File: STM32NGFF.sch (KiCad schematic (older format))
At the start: 30 parts, among them J1 USB_C_Receptacle_USB2.0, J2 2199119-4, U1 MIC5205-3.3YM5, U2 STM32F303CCTx, U3 USBLC6-2SC6, Y1 16MHz

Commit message: Add Correct M.2 Connector, and switch MCU to STM32F303RBTx
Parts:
- removed U2: STM32F303CCTx, Package_QFP:LQFP-48_7x7mm_P0.5mm, symbol MCU_ST_STM32F3:STM32F303CCTx
- added C11: 100n, Capacitor_SMD:C_0603_1608Metric, symbol Device:C_Small
- added U2: STM32F303RBTx, Package_QFP:LQFP-64_10x10mm_P0.5mm, symbol MCU_ST_STM32F3:STM32F303RBTx
- J2: symbol TE_2199119-4:2199119-4 -> Argosy~Research:NASM0-S6701-TP40
- renumbered C3 to C10, C11 to C12, C12 to C13, C4 to C3, C6 to C4, C7 to C6, C8 to C7, C9 to C8, C10 to C9
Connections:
- net labels added: PC0, PC1, PC10, PC11, PC12, PC13, PC4, PC5, PC6, PC7, PC8, PC9, PD2, PF4
- net labels removed: NRST
- wire segments 163 -> 196
- no-connect marks 3 -> 4
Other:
- moved on the sheet: C1, C10, C12, C13, C2, C3, C4, C5, C6, C7, C8, C9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

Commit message: Routed and shaped PCB
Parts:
- removed C10: 10uf, Capacitor_SMD:C_0603_1608Metric, symbol Device:C_Small
- removed C4: 100nF, Capacitor_SMD:C_0603_1608Metric, symbol Device:C_Small
- removed J1: USB_C_Receptacle_USB2.0, Connector_USB:USB_C_Receptacle_HRO_TYPE-C-31-M-12, symbol Connector:USB_C_Receptacle_USB2.0
- added C12, C7: 100nF, Capacitor_SMD:C_0603_1608Metric, symbol Device:C_Small
- added C14: 10uf, Capacitor_SMD:C_0603_1608Metric, symbol Device:C_Small
- added J2, J4: S4B-PH-K-S(LF)(SN), JST:S4B-PH-K-S_LF_SN, symbol JST:S4B-PH-K-S(LF)(SN)
- added J3: HRO_TYPE-C-31-M-12, Type-C:HRO-TYPE-C-31-M-12-Assembly, symbol Type-C:HRO-TYPE-C-31-M-12
- added R7: 5.11k, Capacitor_SMD:C_0603_1608Metric, symbol Device:R_Small
- added R8: 1M, Capacitor_SMD:C_0603_1608Metric, symbol Device:R_Small
- added U1: 74LVC1G17, Package_TO_SOT_SMD:SOT-23-5, symbol 74xGxx:74LVC1G17
- J1: renamed from J2; value 2199119-4 -> NASMO-S6701-TP40; footprint TE:TE_2199119-4 -> Argosy Research:NASMO-S6701-TP40; symbol Argosy~Research:NASM0-S6701-TP40 -> Argosy_Research:NASM0-S6701-TP40; Comment 2199119-4 -> NASMO-S6701-TP40
- R4: value 1M -> 470
- R5: value 5.11k -> 1M
- renumbered C11 to C10, C12 to C11, C5 to C4, C6 to C5, C7 to C6, U1 to U2, U2 to U3, U3 to U4
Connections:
- net labels added: LED_3V3, LED_5V, LED_DATA, PC2, VBUS
- net labels removed: PB13
- wire segments 196 -> 283
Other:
- note added: "Addressable LED Support"
- note added: "SOM USB JST Connector"
- note added: "USB Daughterboard"
- note removed: "USB ESD Protection"
- note removed: "USB-C Connection"
- moved on the sheet: C10, C11, C13, C3, C4, C5, C6, C8, C9, L1, U2, U4

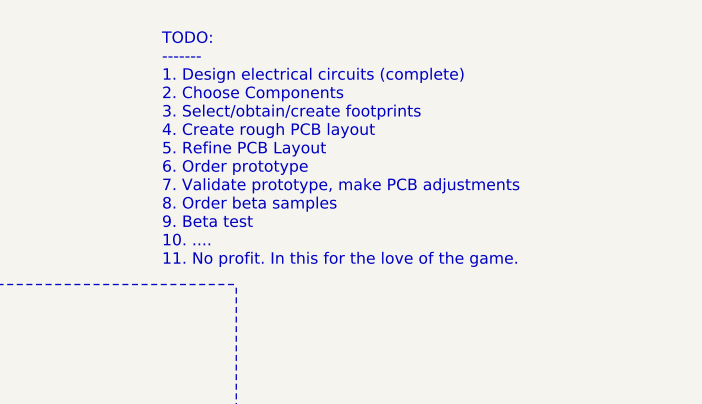
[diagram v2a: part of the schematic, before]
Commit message: Updated TODO list in schematic
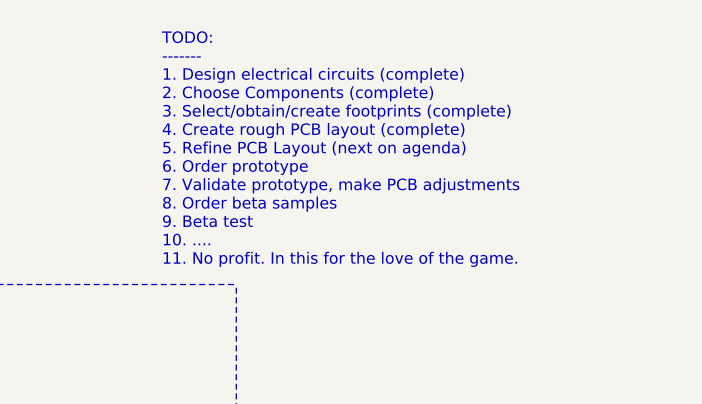
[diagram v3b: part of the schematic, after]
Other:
- note added: "TODO:\n-------\n1. Design electrical circuits (complete)\n2. Choose Components (complete)\n3. Select/obtain/create footprints (complete)\n4. Create rough PCB layout (complete)\n5. Refine PCB Layout (next on agenda)\n6. Order prototype\n7. Validate prototype, make PCB adjustments\n8. Order beta samples\n9. Beta test\n10. ....\n11. No profit. In this for the love of the game."
- note removed: "TODO:\n-------\n1. Design electrical circuits (complete)\n2. Choose Components\n3. Select/obtain/create footprints\n4. Create rough PCB layout\n5. Refine PCB Layout\n6. Order prototype\n7. Validate prototype, make PCB adjustments\n8. Order beta samples\n9. Beta test\n10. ....\n11. No profit. In this for the love of the game."
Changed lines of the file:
@@
 BOOT0 Pulldown
 Text Notes 9300 1575 0    50   ~ 0
-TODO:\n-------\n1. Design electrical circuits (complete)\n2. Choose Components\n3. Select/obtain/create footprints\n4. Create rough PCB layout\n5. Refine PCB Layout\n6. Order prototype\n7. Validate prototype, make PCB adjustments\n8. Order beta samples\n9. Beta test\n10. ....\n11. No profit. In this for the love of the game.
+TODO:\n-------\n1. Design electrical circuits (complete)\n2. Choose Components (complete)\n3. Select/obtain/create footprints (complete)\n4. Create rough PCB layout (complete)\n5. Refine PCB Layout (next on agenda)\n6. Order prototype\n7. Validate prototype, make PCB adjustments\n8. Order beta samples\n9. Beta test\n10. ....\n11. No profit. In this for the love of the game.
 Text Notes 6900 5250 0    50   ~ 0
 5V to 3.3V Conversion Using MIC5205

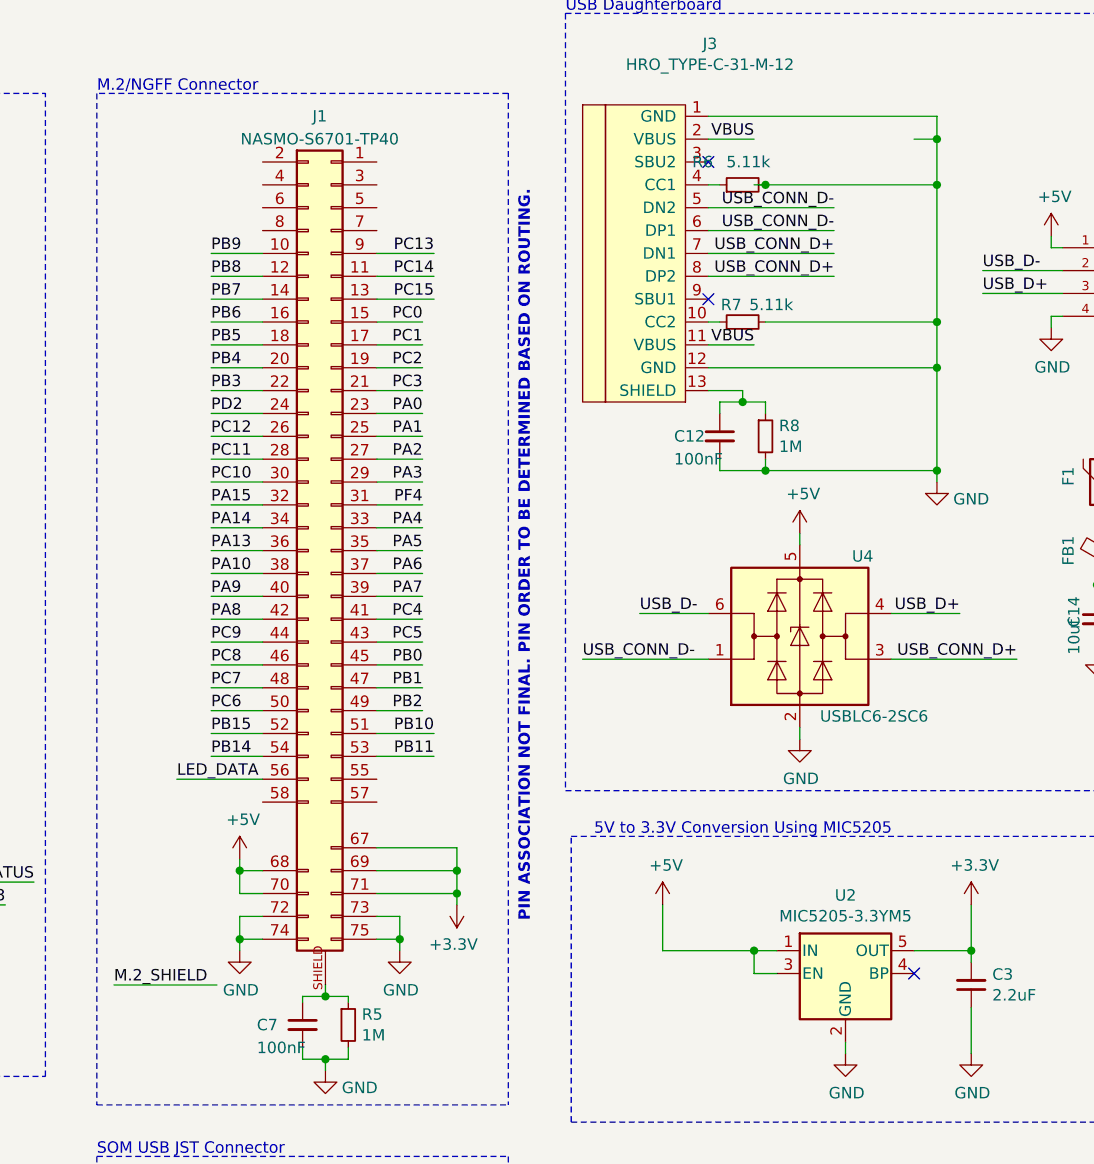
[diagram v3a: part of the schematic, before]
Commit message: Updated 3.3V Generator and NGFF footprint
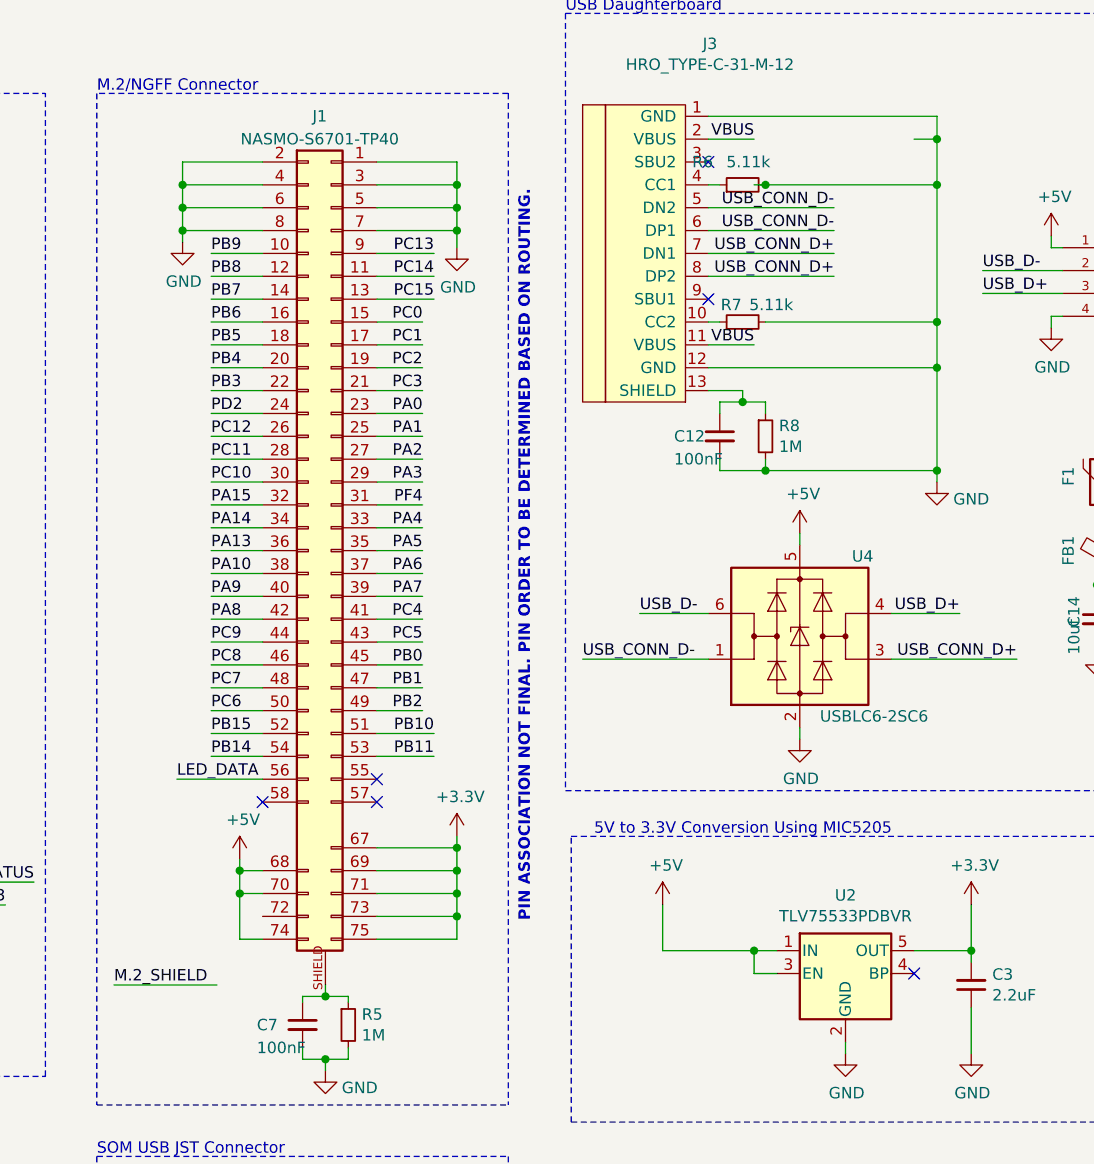
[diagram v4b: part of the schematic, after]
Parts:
- U2: value MIC5205-3.3YM5 -> TLV75533PDBVR
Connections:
- net +3V3: now also J1.73 (Pin_73), J1.75 (Pin_75)
- net +5V: now also J1.74 (Pin_74)
- net GND: now also J1.1 (Pin_1), J1.2 (Pin_2), J1.3 (Pin_3), J1.4 (Pin_4), J1.5 (Pin_5), J1.6 (Pin_6), J1.7 (Pin_7), J1.8 (Pin_8); no longer J1.72 (Pin_72), J1.73 (Pin_73), J1.74 (Pin_74), J1.75 (Pin_75)
- no-connect marks 4 -> 7
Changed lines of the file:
@@
 P 8000 5850
 F 0 "U2" H 8000 6192 50  0000 C CNN
-F 1 "MIC5205-3.3YM5" H 8000 6101 50  0000 C CNN
+F 1 "TLV75533PDBVR" H 8000 6101 50  0000 C CNN
 F 2 "Package_TO_SOT_SMD:SOT-23-5" H 8000 6175 50  0001 C CNN
 F 3 "http://ww1.microchip.com/downloads/en/DeviceDoc/20005785A.pdf" H 8000 5850 50  0001 C CNN
@@
 L power:+3.3V #PWR025
 U 1 1 602275CF
-P 6300 5550
-F 0 "#PWR025" H 6300 5400 50  0001 C CNN
-F 1 "+3.3V" H 6315 5723 50  0000 C CNN
-F 2 "" H 6300 5550 50  0001 C CNN
-F 3 "" H 6300 5550 50  0001 C CNN
-	1    6300 5550
-	-1   0    0    1
-$EndComp
-Wire Wire Line
-	6300 5550 6300 5500
+P 6300 5250
+F 0 "#PWR025" H 6300 5100 50  0001 C CNN
+F 1 "+3.3V" H 6315 5423 50  0000 C CNN
+F 2 "" H 6300 5250 50  0001 C CNN
+F 3 "" H 6300 5250 50  0001 C CNN
+	1    6300 5250
+	1    0    0    -1
+$EndComp
 Wire Wire Line
 	6300 5400 5950 5400
@@
 Wire Wire Line
 	6300 5500 6300 5400
-$Comp
-L power:GND #PWR024
-U 1 1 60271EDF
-P 6050 5750
-F 0 "#PWR024" H 6050 5500 50  0001 C CNN
-F 1 "GND" H 6055 5577 50  0000 C CNN
-F 2 "" H 6050 5750 50  0001 C CNN
-F 3 "" H 6050 5750 50  0001 C CNN
-	1    6050 5750
-	1    0    0    -1
-$EndComp
-Wire Wire Line
-	5450 5600 5350 5600
-Wire Wire Line
-	5350 5600 5350 5700
-Wire Wire Line
-	5450 5700 5350 5700
-Connection ~ 5350 5700
-Wire Wire Line
-	5350 5700 5350 5750
-Wire Wire Line
-	5950 5600 6050 5600
-Wire Wire Line
-	6050 5600 6050 5700
-Wire Wire Line
-	5950 5700 6050 5700
-Connection ~ 6050 5700
-Wire Wire Line
-	6050 5700 6050 5750
-$Comp
-L power:GND #PWR020
-U 1 1 60295BF3
-P 5350 5750
-F 0 "#PWR020" H 5350 5500 50  0001 C CNN
-F 1 "GND" H 5355 5577 50  0000 C CNN
-F 2 "" H 5350 5750 50  0001 C CNN
-F 3 "" H 5350 5750 50  0001 C CNN
-	1    5350 5750
-	1    0    0    -1
-$EndComp
 Wire Wire Line
 	5450 5500 5350 5500
@@
 Text Label 5075 5000 0    50   ~ 0
 LED_DATA
+$Comp
+L power:GND #PWR?
+U 1 1 5FBB4348
+P 5100 2650
+F 0 "#PWR?" H 5100 2400 50  0001 C CNN
+F 1 "GND" H 5105 2477 50  0000 C CNN
+F 2 "" H 5100 2650 50  0001 C CNN
+F 3 "" H 5100 2650 50  0001 C CNN
+	1    5100 2650
+	1    0    0    -1
+$EndComp
+$Comp
+L power:GND #PWR?
+U 1 1 5FBB4ED7
+P 6300 2675
+F 0 "#PWR?" H 6300 2425 50  0001 C CNN
+F 1 "GND" H 6305 2502 50  0000 C CNN
+F 2 "" H 6300 2675 50  0001 C CNN
+F 3 "" H 6300 2675 50  0001 C CNN
+	1    6300 2675
+	1    0    0    -1
+$EndComp
+Wire Wire Line
+	5450 2300 5100 2300
+Wire Wire Line
+	5100 2300 5100 2400
+Wire Wire Line
+	5450 2400 5100 2400
+Connection ~ 5100 2400
+Wire Wire Line
+	5100 2400 5100 2500
+Wire Wire Line
+	5450 2500 5100 2500
+Connection ~ 5100 2500
+Wire Wire Line
+	5100 2500 5100 2600
+Wire Wire Line
+	5450 2600 5100 2600
+Connection ~ 5100 2600
+Wire Wire Line
+	5100 2600 5100 2650
+Wire Wire Line
+	5950 2300 6300 2300
+Wire Wire Line
+	6300 2300 6300 2400
+Wire Wire Line
+	5950 2600 6300 2600
+Connection ~ 6300 2600
+Wire Wire Line
+	6300 2600 6300 2675
+Wire Wire Line
+	5950 2500 6300 2500
+Connection ~ 6300 2500
+Wire Wire Line
+	6300 2500 6300 2600
+Wire Wire Line
+	5950 2400 6300 2400
+Connection ~ 6300 2400
+Wire Wire Line
+	6300 2400 6300 2500
+Wire Wire Line
+	5350 5500 5350 5700
+Wire Wire Line
+	5350 5700 5450 5700
+Connection ~ 5350 5500
+Connection ~ 6300 5300
+Wire Wire Line
+	6300 5250 6300 5300
+Wire Wire Line
+	5950 5700 6300 5700
+Wire Wire Line
+	6300 5500 6300 5600
+Wire Wire Line
+	5950 5600 6300 5600
+Connection ~ 6300 5600
+Wire Wire Line
+	6300 5600 6300 5700
+NoConn ~ 5950 5000
+NoConn ~ 5950 5100
+NoConn ~ 5450 5100
 $EndSCHEMATC

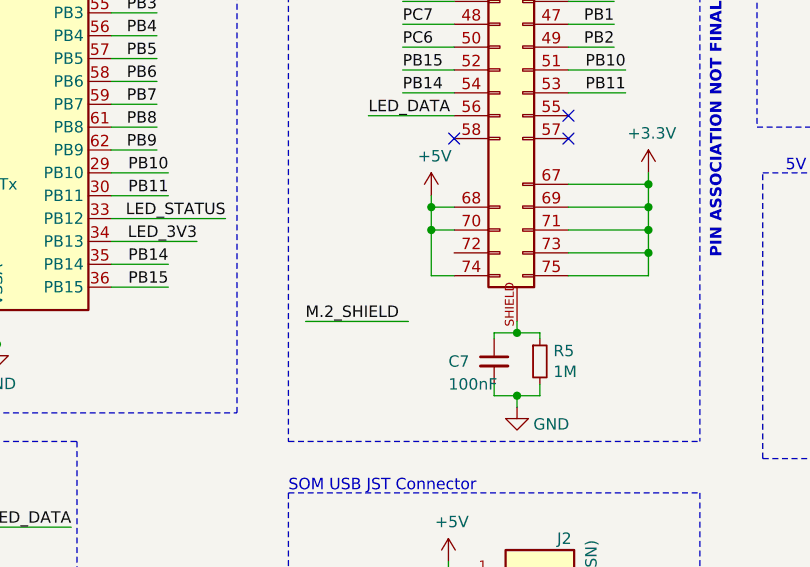
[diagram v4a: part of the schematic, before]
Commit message: Updated NGFF pinout for 3.3V, 5V, and GND
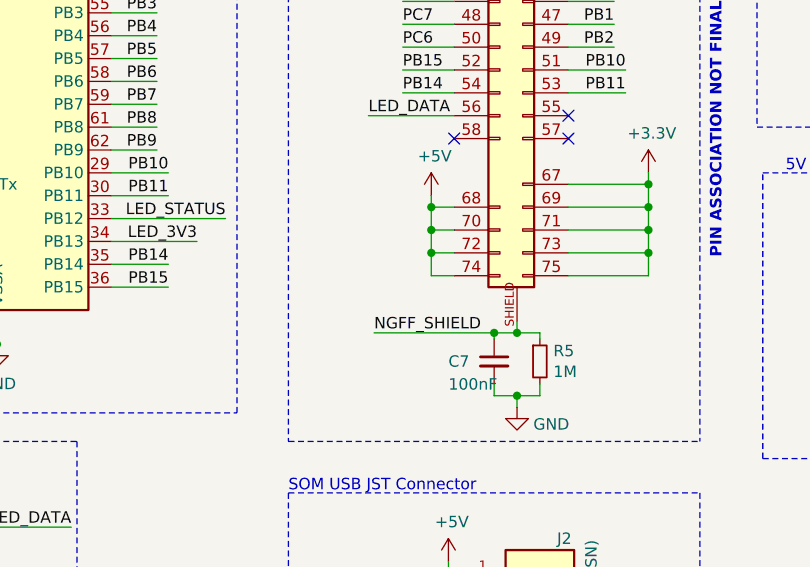
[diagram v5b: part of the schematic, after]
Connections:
- net +5V: now also J1.72 (Pin_72)
- net NGFF_SHIELD: now reaches C7.1, J1.SHIELD (Pin_SHIELD), R5.1
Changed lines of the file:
@@
 Wire Wire Line
 	4200 4050 3950 4050
-Text Label 4800 5900 0    50   ~ 0
-M.2_SHIELD
-Wire Wire Line
-	4800 5900 5250 5900
+Text Label 5100 5950 0    50   ~ 0
+NGFF_SHIELD
+Wire Wire Line
+	5100 5950 5625 5950
 $Comp
 L power:+3.3V #PWR025
@@
 LED_DATA
 $Comp
-L power:GND #PWR?
+L power:GND #PWR0101
 U 1 1 5FBB4348
 P 5100 2650
-F 0 "#PWR?" H 5100 2400 50  0001 C CNN
+F 0 "#PWR0101" H 5100 2400 50  0001 C CNN
 F 1 "GND" H 5105 2477 50  0000 C CNN
 F 2 "" H 5100 2650 50  0001 C CNN
@@
 $EndComp
 $Comp
-L power:GND #PWR?
+L power:GND #PWR0102
 U 1 1 5FBB4ED7
 P 6300 2675
-F 0 "#PWR?" H 6300 2425 50  0001 C CNN
+F 0 "#PWR0102" H 6300 2425 50  0001 C CNN
 F 1 "GND" H 6305 2502 50  0000 C CNN
 F 2 "" H 6300 2675 50  0001 C CNN
@@
 	6300 2400 6300 2500
 Wire Wire Line
-	5350 5500 5350 5700
+	5350 5500 5350 5600
 Wire Wire Line
 	5350 5700 5450 5700
@@
 NoConn ~ 5950 5100
 NoConn ~ 5450 5100
+Wire Wire Line
+	5350 5600 5450 5600
+Connection ~ 5350 5600
+Wire Wire Line
+	5350 5600 5350 5700
+Connection ~ 5625 5950
 $EndSCHEMATC
